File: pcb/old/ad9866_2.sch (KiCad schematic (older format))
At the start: 104 parts, among them CN1 MEC6-140_CONNECTOR_BEMICRO, CON1 USB-MICRO-B, P1 CONN_2, P10 CONN_1, P2 CONN_10X2, P3 CONN_1, P4 CONN_5X2, P5V0 CONN_1, P6 Coaxial_Connector, P7 Coaxial_Connector, P8 CONN_2, P9 CONN_1, Q1 Si2301, T1 TRANSF_ADT2, T2 TRANSF_ADT8, U1 NCP1117ST33T3G, U2 NCP1117ST33T3G, U3 Si510, U4 AD9866BCPZ, U5 NCP1117ST33T3G, U6 25AA02E48T-I/OT

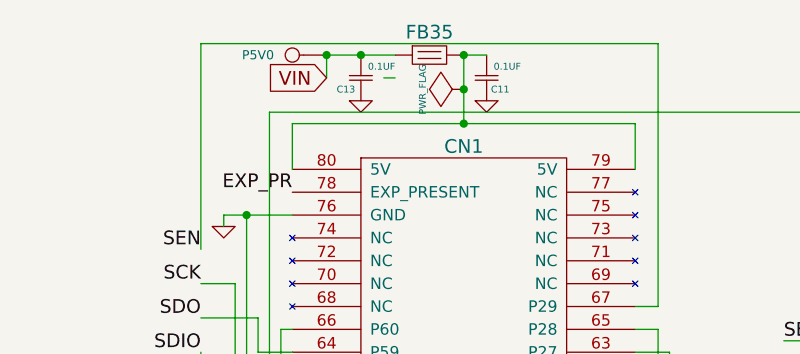
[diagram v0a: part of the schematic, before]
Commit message: Added doc link for ferrite beads.
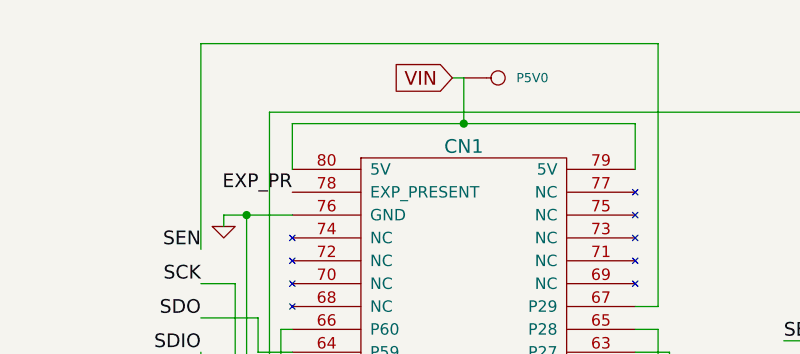
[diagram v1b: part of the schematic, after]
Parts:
- removed C11, C13: 0.1UF, symbol Csmall
- removed FB35: FB, symbol FB
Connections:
- net VIN: now also CN1.79 (5V), CN1.80 (5V)
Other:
- moved on the sheet: P5V0
